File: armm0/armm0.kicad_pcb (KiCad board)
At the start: 2 copper layers, 25.4 x 52.1 mm, 23 parts, among them J1 Conn_02x10_Odd_Even, J4 Conn_02x08_Odd_Even, J5 Conn_02x08_Odd_Even, J6 Conn_01x05_Male, J7 Conn_01x05_Male, J8 Conn_01x03_Male, U1 STM32F070F6Px, U2 LD1117S33TR_SOT223

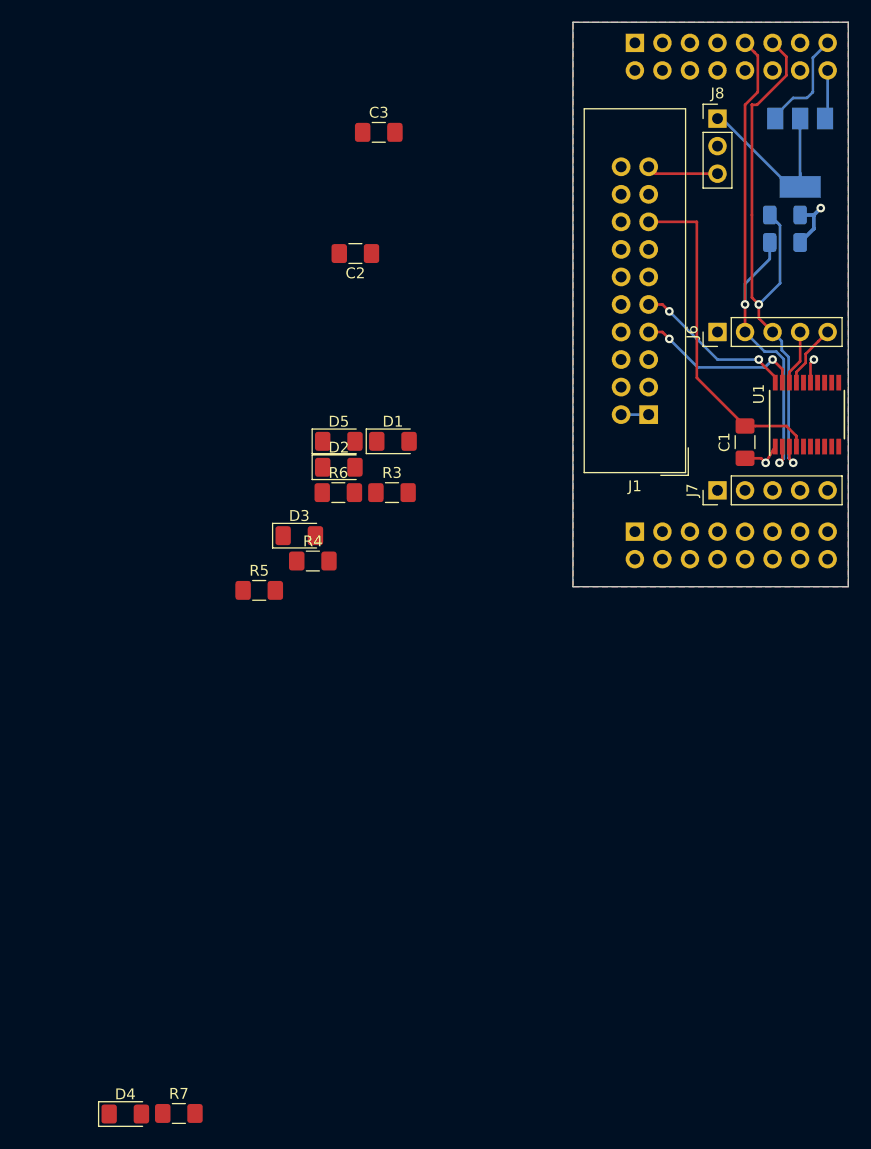
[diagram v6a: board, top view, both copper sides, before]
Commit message: sch: Use resistor array for debug leds
Signed-off-by: Ben Lancaster <bdl@live.co.uk>
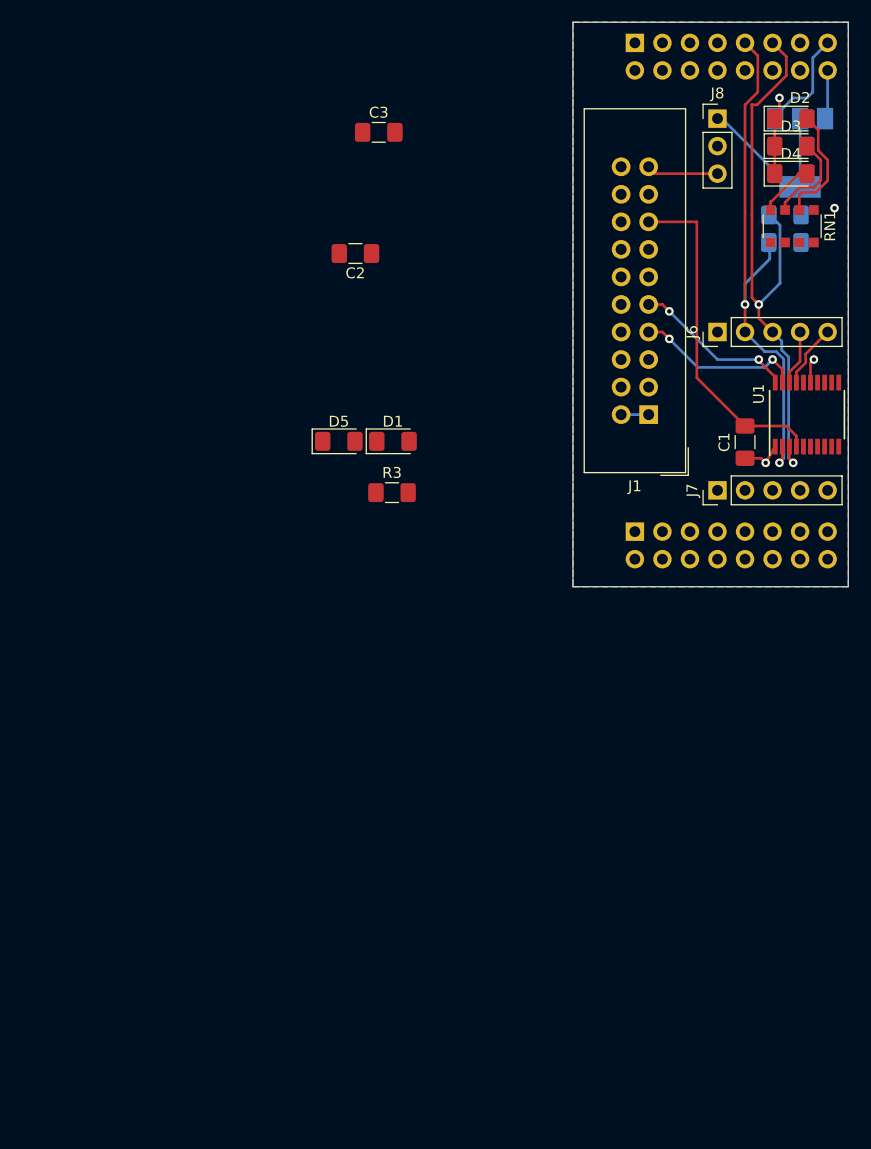
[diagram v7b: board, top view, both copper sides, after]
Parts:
- removed R4, R5, R6, R7: R, Resistor_SMD:R_1206_3216Metric_Pad1.42x1.75mm_HandSolder
- added RN1: R_Network04, Resistor_SMD:R_Array_Convex_4x1206, F.Cu at (95.2, 49.9)
- R1, R2: footprint Resistor_SMD:R_1206_3216Metric -> Resistor_SMD:R_1206_3216Metric_Pad1.42x1.75mm_HandSolder
- moved D4 106.3 mm to (95.0, 45.1)
- moved D3 57.9 mm to (95.0, 42.5)
- moved D2 52.7 mm to (95.0, 40.0)
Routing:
- net Net-(D2-Pad2): track 0.00 -> 11.0 mm
- net Net-(D3-Pad2): track 0.00 -> 8.53 mm
- net GND: track 15.8 -> 23.3 mm, vias 2 -> 3
- net Net-(D4-Pad2): track 0.00 -> 5.36 mm
- net +3V3: track 5.23 -> 0.00 mm

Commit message: pcb: All connected
Signed-off-by: Ben Lancaster <bdl@live.co.uk>
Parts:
- C2, C3: moved to B.Cu
- moved D5 47.2 mm to (95.0, 47.6)
- moved C3 47.0 mm to (97.4, 65.4)
- moved C2 45.7 mm to (97.6, 68.6), turned to 0 degrees
- moved R3 43.3 mm to (83.6, 39.4), turned to 180 degrees
- moved D1 36.4 mm to (78.3, 39.4)
- moved RN1 3.41 mm to (95.2, 53.3)
- moved J1 3.17 mm to (81.9, 70.5)
- moved R1 0.63 mm to (94.5, 52.1)
- moved R2 0.63 mm to (94.5, 49.5)
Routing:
- net +3V3: track 0.00 -> 41.3 mm, vias 1 -> 4
- net STLINK_3V3: track 9.15 -> 35.9 mm
- net GND: track 23.3 -> 44.1 mm
- net Net-(D5-Pad2): track 0.00 -> 9.62 mm
- net NRST: track 31.2 -> 25.4 mm
- net Net-(D4-Pad2): track 5.36 -> 10.0 mm
- net Net-(D3-Pad2): track 8.53 -> 12.3 mm
- net Net-(D2-Pad2): track 11.0 -> 14.0 mm
- net Net-(D1-Pad2): track 0.00 -> 2.30 mm
- net SWDIO: track 15.6 -> 14.3 mm, vias 2 -> 1
- net SWCLK: track 15.0 -> 13.9 mm, vias 2 -> 1
